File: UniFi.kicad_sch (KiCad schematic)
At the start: 67 parts, among them J1 OLED, J2 MJ-4PP-9 TRRS, SW1 SW_PUSH-MX_W_LED, SW10 SW_PUSH-MX_W_LED, SW11 SW_PUSH-MX_W_LED, SW12 SW_PUSH-MX_W_LED, SW13 SW_PUSH-MX_W_LED, SW14 SW_PUSH-MX_W_LED, SW15 SW_PUSH-MX_W_LED, SW16 SW_PUSH-MX_W_LED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

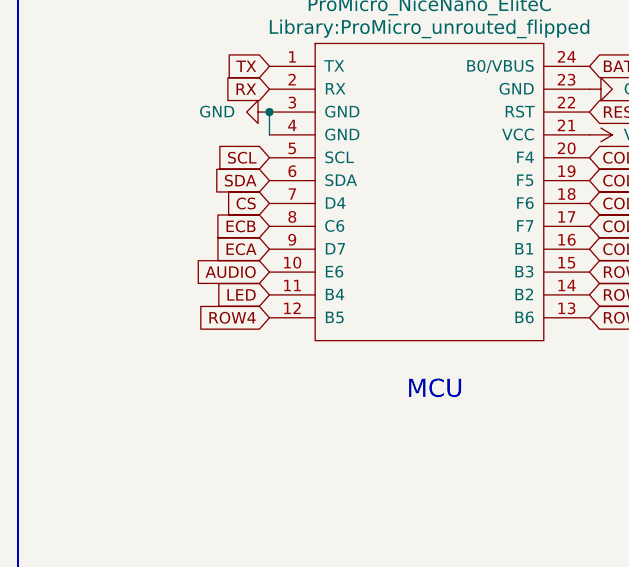
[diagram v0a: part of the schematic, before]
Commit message: Updated pins
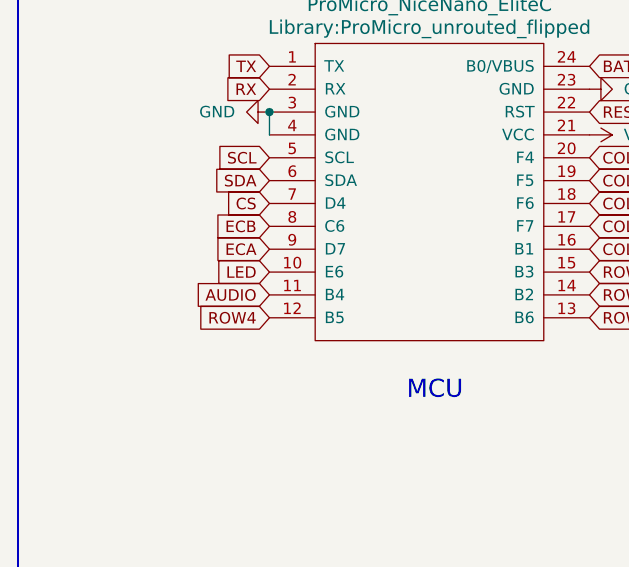
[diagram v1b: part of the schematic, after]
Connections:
- net AUDIO: now also U1.11 (B4); no longer U1.10 (E6)
- net LED: now also U1.10 (E6); no longer U1.11 (B4)
